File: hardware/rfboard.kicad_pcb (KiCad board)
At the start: 2 copper layers, 28.4 x 34.6 mm, 20 parts, among them J1 10118194-0001LF, J2 CONN_01X11, J3 CONN_01X11, P2 CONN_01X03, P3 CONN_01X04, P5 CONN_01X01, U1 SAMD21E18, U2 RFM69CW-915MHZ, U3 MIC5504-3.3YM5-T5

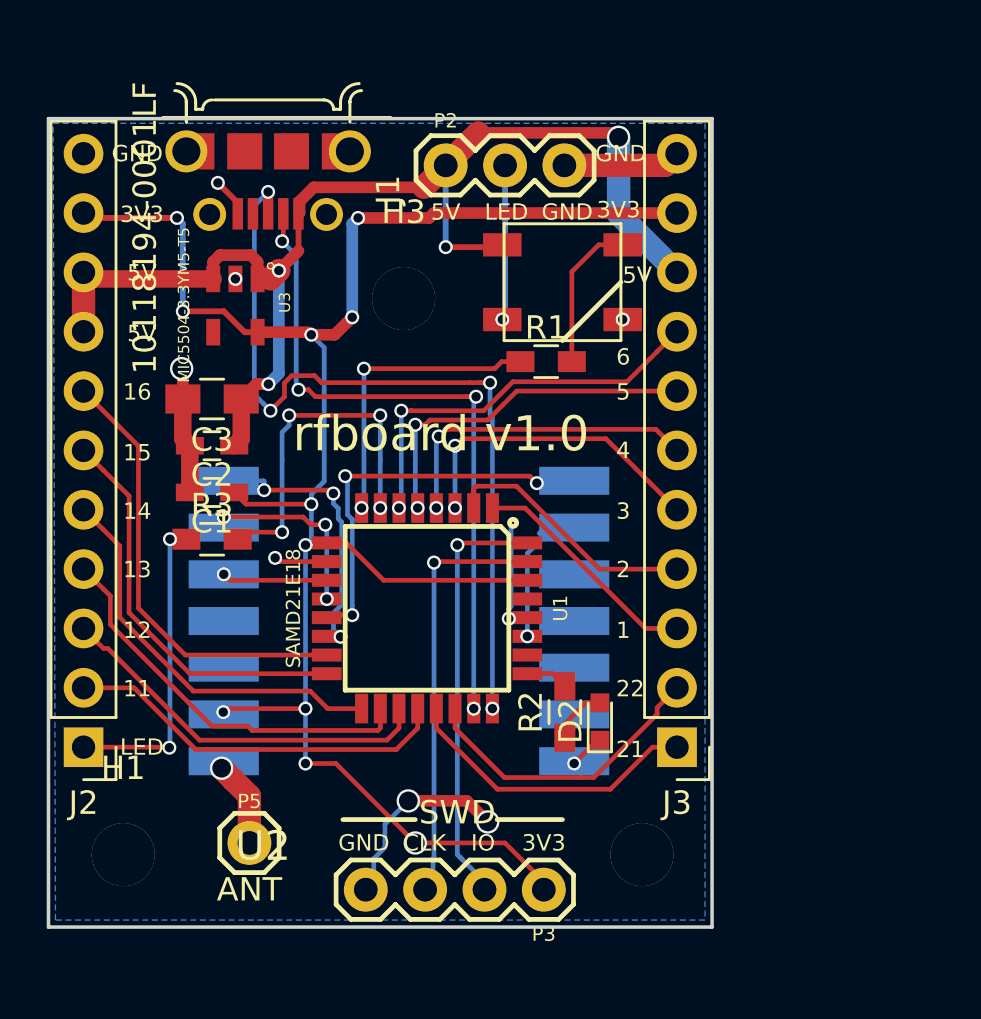
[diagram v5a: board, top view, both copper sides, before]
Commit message: Hardware revision 1.1:
- Add a buffer to bump up the signal to the serial LED to 5V
- Switch SWD progamming input voltage to 5V
- Add a reset button
- Remove two less-useful pins
- Make the board two breadboard rows smaller
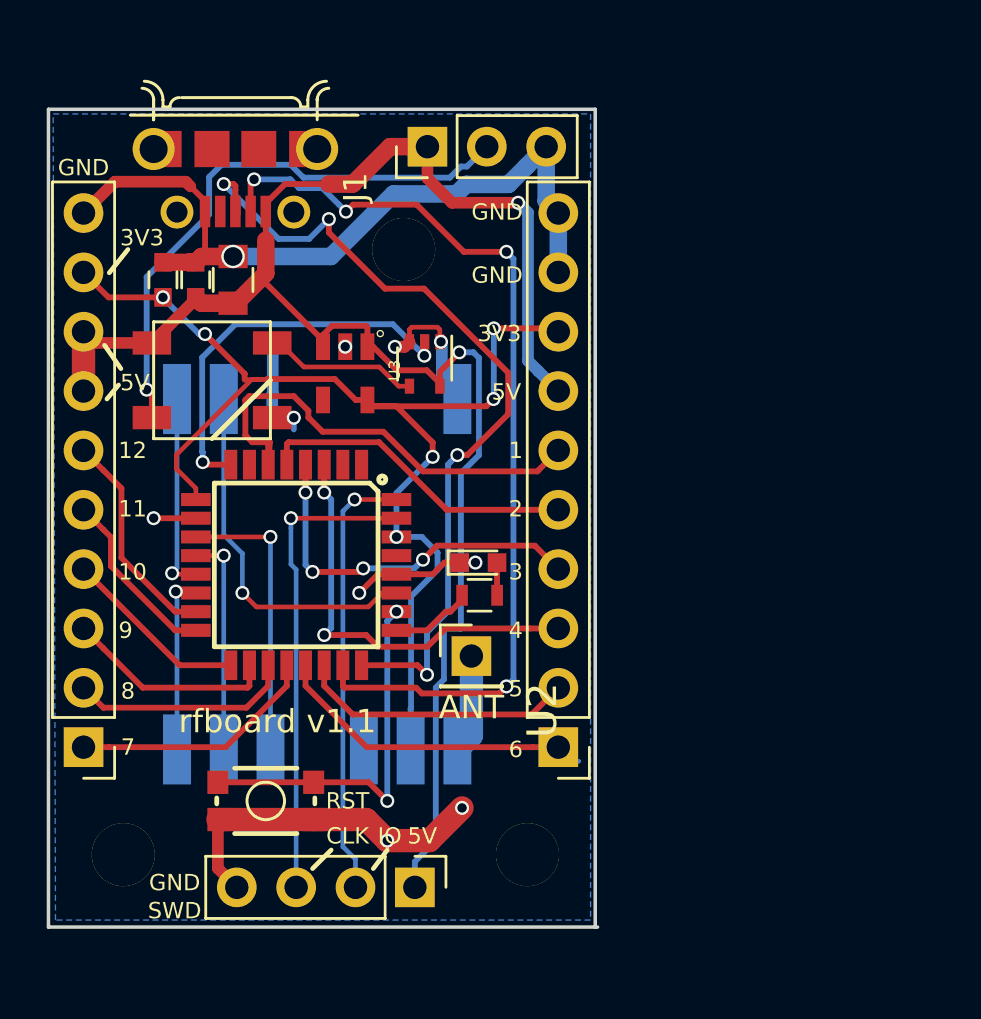
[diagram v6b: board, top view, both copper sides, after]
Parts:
- removed R1, R3: 220, Resistors_SMD:R_0603_HandSoldering
- added S1: MOMENTARY-SWITCH-SPST-SMD-4.6X2.8MM, SparkFun-Switches:TACTILE_SWITCH_SMD_4.6X2.8MM, F.Cu at (115.3, 157.2)
- added U4: 74LVC1G125, TO_SOT_Packages_SMD:SOT-353_SC-70-5, F.Cu at (122.1, 138.5)
- C1, C2: footprint Capacitors_SMD:C_0603_HandSoldering -> Capacitors_SMD:C_0603
- C3: footprint Capacitors_SMD:C_0805_HandSoldering -> Capacitors_SMD:C_0805
- J2, J3: value CONN_01X11 -> Conn_01x10; footprint Pin_Headers:Pin_Header_Straight_1x11_Pitch2.54mm -> Pin_Headers:Pin_Header_Straight_1x10_Pitch2.54mm
- P2: footprint Sparkfun-Connectors:1X03 -> Pin_Headers:Pin_Header_Straight_1x03_Pitch2.54mm
- P3: footprint Sparkfun-Connectors:1X04 -> Pin_Headers:Pin_Header_Straight_1x04_Pitch2.54mm
- P5: footprint Sparkfun-Connectors:1X01 -> Pin_Headers:Pin_Header_Straight_1x01_Pitch2.54mm
- R2: footprint Resistors_SMD:R_0603_HandSoldering -> Resistors_SMD:R_0603
- U2: footprint homebrew:RFM69CW-XXXS2_ -> homebrew:RFM69CW-minimalpads
- moved D1 15.6 mm to (113.0, 139.2)
- moved P5 12.4 mm to (124.1, 151.0)
- moved C1 9.34 mm to (110.9, 134.9), turned to 90 degrees
- moved D2 8.56 mm to (124.4, 147.0), turned to 0 degrees
- moved C2 7.13 mm to (112.3, 134.9), turned to 90 degrees
- moved R2 6.19 mm to (124.5, 148.4), turned to 180 degrees
- moved U1 5.90 mm to (116.6, 147.1)
- moved U3 5.52 mm to (118.7, 138.9)
- moved P3 5.52 mm to (121.7, 160.9), turned to 270 degrees
- moved C3 5.18 mm to (113.9, 134.9), turned to 90 degrees
- moved J3 5.08 mm to (127.8, 154.9)
- moved H2 4.90 mm to (126.5, 159.5)
- moved U2 4.03 mm to (117.5, 147.5), turned to 90 degrees
- moved H3 2.10 mm to (121.2, 133.6)
- moved J1 1.40 mm to (114.0, 129.3)
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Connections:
- J2 pad 1: Net-(J2-Pad1) -> L1
- J2 pad 10: +3V3 -> GND
- J2 pad 2: L1 -> L2
- J2 pad 3: L2 -> L3
- J2 pad 4: L3 -> L4
- J2 pad 5: L4 -> L5
- J2 pad 6: L5 -> L6
- J2 pad 7: L6 -> +5V
- J2 pad 9: +5V -> +3V3
- J3 pad 10: +3V3 -> GND
- J3 pad 7: R7 -> +5V
- J3 pad 8: R8 -> +3V3
- J3 pad 9: +5V -> GND
- P3 pad 1: +3V3 -> +5V
- U1 pad 1: R3 -> Net-(U1-Pad1)
- U1 pad 2: R4 -> Net-(U1-Pad2)
- U1 pad 26: Net-(U1-Pad26) -> RESET_SW
- U1 pad 3: R5 -> R3
- U1 pad 4: R6 -> R4
- U1 pad 5: R7 -> R5
- U1 pad 6: R8 -> R6
- U1 pad 7: LED_EXTERNAL_2 -> Net-(U1-Pad7)
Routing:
- net GND: track 29.1 -> 62.6 mm, vias 9 -> 10
- net +3V3: track 83.3 -> 53.8 mm, vias 11 -> 6
- net +5V: track 53.7 -> 76.1 mm, vias 4 -> 2
- net LED_EXTERNAL: track 6.70 -> 24.4 mm
- net R8: track 17.4 -> 0.00 mm, vias 2 -> 0
- net RESET_SW: track 0.00 -> 15.8 mm, vias 0 -> 2
- net R7: track 15.4 -> 0.00 mm, vias 2 -> 0
- net LED_EXTERNAL_2: track 15.0 -> 0.00 mm, vias 4 -> 0
- net Net-(J2-Pad1): track 13.3 -> 0.00 mm, vias 2 -> 0
- net USB_D-: track 29.0 -> 40.8 mm
- net L6: track 19.2 -> 9.41 mm
- net L5: track 17.3 -> 7.67 mm
- net L4: track 17.2 -> 8.01 mm
- net RADIO_MISO: track 17.6 -> 8.58 mm, vias 3 -> 1
- net RADIO_DIO0: track 7.61 -> 15.7 mm
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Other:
- board size 28.4 x 34.6 mm -> 23.5 x 35 mm
- board text added: "10"
- board text added: "2812"
- board text added: "7"
- board text added: "8"
- board text added: "9"
- board text added: "BUF"
- board text added: "G"
- board text added: "REG"
- board text added: "RST"
- board text added: "SW"
- board text added: "rfboard v1.1"
- board text removed: "13"
- board text removed: "14"
- board text removed: "15"
- board text removed: "16"
- board text removed: "21"
- board text removed: "22"
- board text removed: "rfboard v1.0"

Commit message: Hardware revision 1.2:
- Add pullup resistors for doing I2C
- Added a helical antenna (untested)
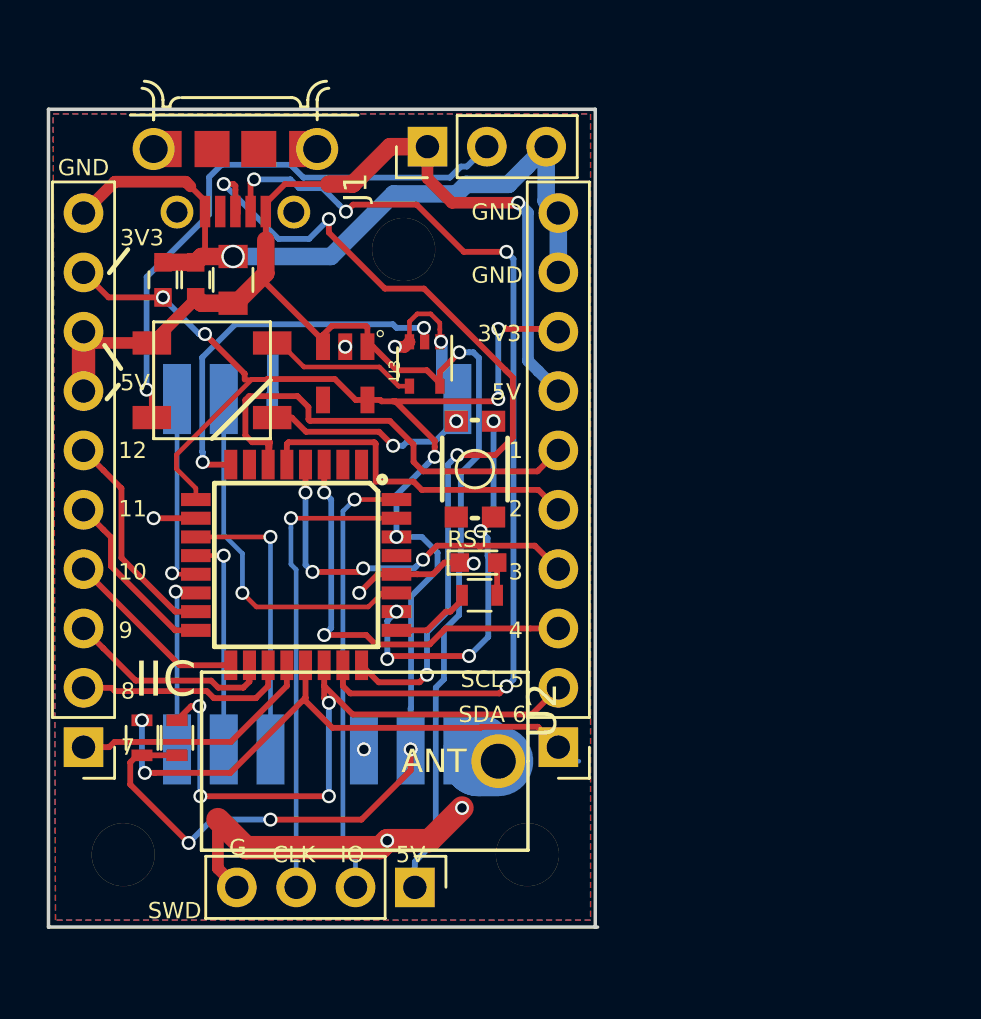
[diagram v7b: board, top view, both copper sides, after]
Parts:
- removed P5: CONN_01X01, Pin_Headers:Pin_Header_Straight_1x01_Pitch2.54mm
- added AE1: Antenna, homebrew:helical_antenna_915mhz_hole, F.Cu at (125.2, 155.5)
- added R1: 4k7, Resistors_SMD:R_0603, F.Cu at (110.0, 154.5)
- added R3: 4k7, Resistors_SMD:R_0603, F.Cu at (111.5, 154.5)
- moved S1 16.8 mm to (124.2, 143.0), turned to 270 degrees
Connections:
- net R1 renamed SDA
- net R2 renamed SCL
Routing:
- net +3V3: track 53.8 -> 71.3 mm, vias 6 -> 9
- net SCL: track 12.7 -> 28.0 mm, vias 0 -> 4
- net SDA: track 13.0 -> 23.9 mm, vias 0 -> 2
- net GND: track 62.6 -> 71.0 mm, vias 10 -> 12
- net ANTENNA: track 4.24 -> 2.20 mm
- net USB_D+: track 36.2 -> 38.0 mm
- net RESET_SW: track 15.8 -> 17.4 mm, vias 2 -> 5
- net R5: track 13.7 -> 14.7 mm
- net R6: track 20.0 -> 20.5 mm
- net LED_INTERNAL: track 17.0 -> 16.5 mm
- added copper zone on F.Cu, net GND
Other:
- board text added: "IIC"
- board text added: "SCL 5"
- board text added: "SDA 6"
- board text added: "rfboard v1.2"
- board text removed: "5"
- board text removed: "6"
- board text removed: "rfboard v1.1"

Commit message: Hardware revision v1.3:
- Add decoupling caps for micro and radio
- Replace antenna with hole (fix placement slightly)
- Updated to KiCAD v5
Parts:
- added C4: 1uF, Capacitor_SMD:C_0603_1608Metric, F.Cu at (110.5, 144.0)
- added C5: 1uF, Capacitor_SMD:C_0603_1608Metric, F.Cu at (120.5, 155.0)
- AE1: footprint homebrew:helical_antenna_915mhz_hole -> Connector_PinHeader_2.54mm:PinHeader_1x01_P2.54mm_Vertical
- moved AE1 0.30 mm to (125.2, 155.8)
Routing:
- net (no net): track 3.01 -> 0.00 mm
- net GND: track 71.0 -> 73.3 mm, vias 12 -> 13
- net +3V3: track 71.3 -> 73.5 mm
- net +5V: track 75.8 -> 76.4 mm
- net USB_D+: track 38.0 -> 38.6 mm
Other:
- board size 23.5 x 35 mm -> 23.4 x 35 mm
- board text added: "rfboard v1.3"
- board text removed: "rfboard v1.2"
